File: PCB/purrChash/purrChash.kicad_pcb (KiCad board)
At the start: 2 copper layers, 39.5 x 70 mm, 6 parts

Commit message: some layout work - will probably change
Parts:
- added BT1: Battery_Cell, Connector_Wire:SolderWire-0.25sqmm_1x02_P4.2mm_D0.65mm_OD1.7mm, B.Cu at (15.1, 56.0)
- added C1: 10u, Capacitor_SMD:C_0805_2012Metric, B.Cu at (23.5, 59.5)
- added C2: 10u, Capacitor_SMD:C_0805_2012Metric, B.Cu at (26.5, 49.5)
- added C3: 100n, Capacitor_SMD:C_0603_1608Metric, B.Cu at (25.0, 59.5)
- added C4: 1u, Capacitor_SMD:C_0805_2012Metric, B.Cu at (10.5, 59.5)
- added C5: 1u, Capacitor_SMD:C_0805_2012Metric, B.Cu at (15.5, 59.5)
- added C7: 1u, Capacitor_SMD:C_0805_2012Metric, B.Cu at (21.5, 59.5)
- added D1: D_Schottky, Diode_SMD:D_0603_1608Metric, B.Cu at (24.5, 49.5)
- added D2: LED, LED_SMD:LED_2010_5025Metric_Pad1.52x2.65mm_HandSolder, B.Cu at (17.5, 17.5)
- added D3: LED, LED_SMD:LED_0805_2012Metric, B.Cu at (8.50, 17.5)
- added J1: USB4135-GF-A_REVA, Connector_USB:USB_C_Receptacle_GCT_USB4135-GF-A_6P_TopMnt_Horizontal, B.Cu at (13.0, 65.5)
- added M1: Motor_DC_ALT, Connector_Wire:SolderWire-0.25sqmm_1x02_P4.2mm_D0.65mm_OD1.7mm, F.Cu at (25.4, 46.0)
- added Q1: Q_NMOS_GSD, Package_TO_SOT_SMD:SOT-23, B.Cu at (29.5, 50.5)
- added R1: 100k, Resistor_SMD:R_0603_1608Metric, B.Cu at (28.5, 54.0)
- added R2: 1k, Resistor_SMD:R_0603_1608Metric, B.Cu at (20.5, 26.5)
- added R3: 1k, Resistor_SMD:R_0603_1608Metric, B.Cu at (19.0, 26.5)
- added R4: 1k, Resistor_SMD:R_0603_1608Metric, B.Cu at (30.5, 54.0)
- added R5: 5.1k, Resistor_SMD:R_0603_1608Metric, B.Cu at (8.00, 61.0)
- added R6: 5.1k, Resistor_SMD:R_0603_1608Metric, B.Cu at (20.0, 63.5)
- added U1: MSP430FR2110/MSP430FR2111, Package_SO:TSSOP-16_4.4x5mm_P0.65mm, B.Cu at (29.5, 60.0)
- added U2: MCP73811T-420I-OT, Package_TO_SOT_SMD:SOT-23-5, B.Cu at (12.9, 59.5)
- added U3: TPS7A0533PDBZR, Package_TO_SOT_SMD:SOT-23-5, B.Cu at (18.5, 59.5)
- ? (x3): moved to F.Cu
- ? (x2): moved to B.Cu
- moved ? 83.1 mm to (78.5, 27.2), turned to 180 degrees (x3)

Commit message: more pcb work
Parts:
- removed C7: 1u, Capacitor_SMD:C_0805_2012Metric
- added C6: 100n, Capacitor_SMD:C_0603_1608Metric, B.Cu at (43.1, 75.0)
- added D4: LED2, Library:LED_1206_3216Metric_shinethrough, B.Cu at (32.6, 31.2)
- added D5: LED3, Library:LED_1206_3216Metric_shinethrough, B.Cu at (24.7, 37.1)
- added D6: LED4, Library:LED_1206_3216Metric_shinethrough, B.Cu at (30.2, 37.1)
- added R10: 1k, Resistor_SMD:R_0603_1608Metric, B.Cu at (27.6, 32.2)
- added R11: 1k, Resistor_SMD:R_0603_1608Metric, B.Cu at (24.2, 39.3)
- added R12: 1k, Resistor_SMD:R_0603_1608Metric, B.Cu at (30.7, 39.3)
- added R7: 100k, Resistor_SMD:R_0603_1608Metric, B.Cu at (44.5, 64.0)
- added R8: 1k, Resistor_SMD:R_0603_1608Metric, B.Cu at (44.5, 65.5)
- added R9: 1k, Resistor_SMD:R_0603_1608Metric, B.Cu at (27.6, 33.7)
- added TP1: TouchPad, Connector_Wire:SolderWirePad_1x01_SMD_1x2mm, F.Cu at (26.4, 61.5)
- added TP2: TouchPad, Connector_Wire:SolderWirePad_1x01_SMD_1x2mm, F.Cu at (29.1, 55.2)
- added TP3: TouchPad, Connector_Wire:SolderWirePad_1x01_SMD_1x2mm, F.Cu at (22.8, 50.3)
- added TP4: TouchPad, Connector_Wire:SolderWirePad_1x01_SMD_1x2mm, F.Cu at (28.1, 45.9)
- C1, C2: value 10u -> 1u
- C3: value 100n -> 1u; footprint Capacitor_SMD:C_0603_1608Metric -> Capacitor_SMD:C_0805_2012Metric
- C4, C5: value 1u -> 10u
- D1: value D_Schottky -> CHG_LED; footprint Diode_SMD:D_0603_1608Metric -> LED_SMD:LED_0603_1608Metric
- D2: value LED -> D_Schottky; footprint LED_SMD:LED_2010_5025Metric_Pad1.52x2.65mm_HandSolder -> Diode_SMD:D_0603_1608Metric
- D3: value LED -> LED1; footprint LED_SMD:LED_0805_2012Metric -> Library:LED_1206_3216Metric_shinethrough
- M1: moved to B.Cu
- R1: value 100k -> 5.1k
- R2, R3, R4: value 1k -> 5.1k
- R6: value 5.1k -> 1k
- U1: value MSP430FR2110/MSP430FR2111 -> BQ21040DBV; footprint Package_SO:TSSOP-16_4.4x5mm_P0.65mm -> Package_TO_SOT_SMD:SOT-23-6
- U2: value MCP73811T-420I-OT -> TPS7A0533PDBZR
- U3: value TPS7A0533PDBZR -> MSP430FR2110/MSP430FR2111; footprint Package_TO_SOT_SMD:SOT-23-5 -> Package_SO:TSSOP-16_4.4x5mm_P0.65mm
- moved R2 52.8 mm to (35.1, 77.2), turned to 90 degrees
- moved D2 48.6 mm to (39.7, 60.7), turned to -90 degrees
- moved R3 48.1 mm to (30.8, 73.1)
- moved C4 36.9 mm to (43.1, 76.8), turned to 180 degrees
- moved U2 28.5 mm to (37.7, 73.6)
- moved U3 27.3 mm to (43.6, 70.2), turned to 90 degrees
- moved C5 26.3 mm to (41.7, 60.9)
- moved C2 25.3 mm to (34.8, 73.4)
- moved R1 24.6 mm to (20.4, 77.2)
- moved C3 21.4 mm to (37.7, 76.7), turned to 0 degrees
- moved D1 21.2 mm to (31.5, 69.5), turned to 0 degrees
- moved J1 20.2 mm to (27.8, 79.4)
- moved ? 20.2 mm to (14.8, 13.8) (x2)
- moved ? 20.2 mm to (14.7, 13.9)
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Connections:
- C1 pad 1: /3V3 -> /5V_USB
- C2 pad 1: /3V3 -> /VBAT
- C4 pad 1: /5V_USB -> /3V3
- C5 pad 1: /VBAT -> /3V3
- D1 pad 1: /3V3 -> CHG
- D1 pad 2: GND -> /CHG_LED
- D2 pad 1: /LED1_R -> /3V3
- D2 pad 2: /3V3 -> GND
- D3 pad 1: /LED2_R -> /LED1_R
- R1 pad 1: /MOTOR_MCU_R -> /CC2
- R2 pad 1: /LED1_R -> /CC1
- R2 pad 2: /LED_MCU -> GND
- R3 pad 1: /LED2_R -> /ISET
- R3 pad 2: /LED_MCU -> GND
- R4 pad 1: /MOTOR_MCU_R -> /TS
- R4 pad 2: /MOTOR_MCU -> /TS_R
- R5 pad 1: /CC2 -> /TS_R
- R6 pad 1: /CC1 -> /VBAT
- R6 pad 2: GND -> /CHG_LED
- U1 pad 1: unconnected-(U1-P1.1/UCA0CLK/ACLK/C1/A1-Pad1) -> /TS
- U1 pad 2: unconnected-(U1-P1.0/UCA0STE/SMCLK/C0/A1/Veref+-Pad2) -> /VBAT
- U1 pad 3: unconnected-(U1-TEST/SBWTCK-Pad3) -> CHG
- U1 pad 4: unconnected-(U1-NRST/NMI/SBWTDIO-Pad4) -> /ISET
- U1 pad 5: /3V3 -> GND
- U1 pad 6: GND -> /5V_USB
- U2 pad 1: /5V_USB -> /VBAT
- U2 pad 4: /5V_USB -> unconnected-(U2-NC-Pad4)
- U2 pad 5: GND -> /3V3
- U3 pad 1: /VBAT -> unconnected-(U3-P1.1/UCA0CLK/ACLK/C1/A1-Pad1)
- U3 pad 2: GND -> unconnected-(U3-P1.0/UCA0STE/SMCLK/C0/A1/Veref+-Pad2)
- U3 pad 3: /VBAT -> unconnected-(U3-TEST/SBWTCK-Pad3)
- U3 pad 4: unconnected-(U3-NC-Pad4) -> CHG
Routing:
- net /3V3: track 0.00 -> 118.5 mm
- net /LED_MCU1: track 0.00 -> 43.1 mm
- net /LED_MCU2: track 0.00 -> 37.7 mm
- net Net-(U3-P1.5/UCA0CLK/TMS/A5): track 0.00 -> 34.0 mm, vias 0 -> 1
- net Net-(U3-P1.6/UCA0RXD/UCA0SOMI/TB0.1/TDI/TCLK/A6): track 0.00 -> 32.0 mm, vias 0 -> 1
- net Net-(U3-P1.4/UCA0STE/TCK/A4): track 0.00 -> 24.9 mm, vias 0 -> 1
- net Net-(U3-P1.3/UCA0STE/TCK/A4): track 0.00 -> 24.2 mm, vias 0 -> 1
- net /VBAT: track 0.00 -> 21.5 mm
- net CHG: track 0.00 -> 19.4 mm
- net GND: track 0.00 -> 14.8 mm
- net /5V_USB: track 0.00 -> 8.11 mm
- net /CC2: track 0.00 -> 7.98 mm
- net /CC1: track 0.00 -> 7.90 mm
- net /LED1_R: track 0.00 -> 3.64 mm
- net /MOTOR_MCU_R: track 0.00 -> 3.31 mm
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- added copper zone on B.Cu, net GND
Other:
- outline, holes or cut-outs redrawn
- board text added: "&"
- board text added: "GalH"
- board text added: "TalyR"

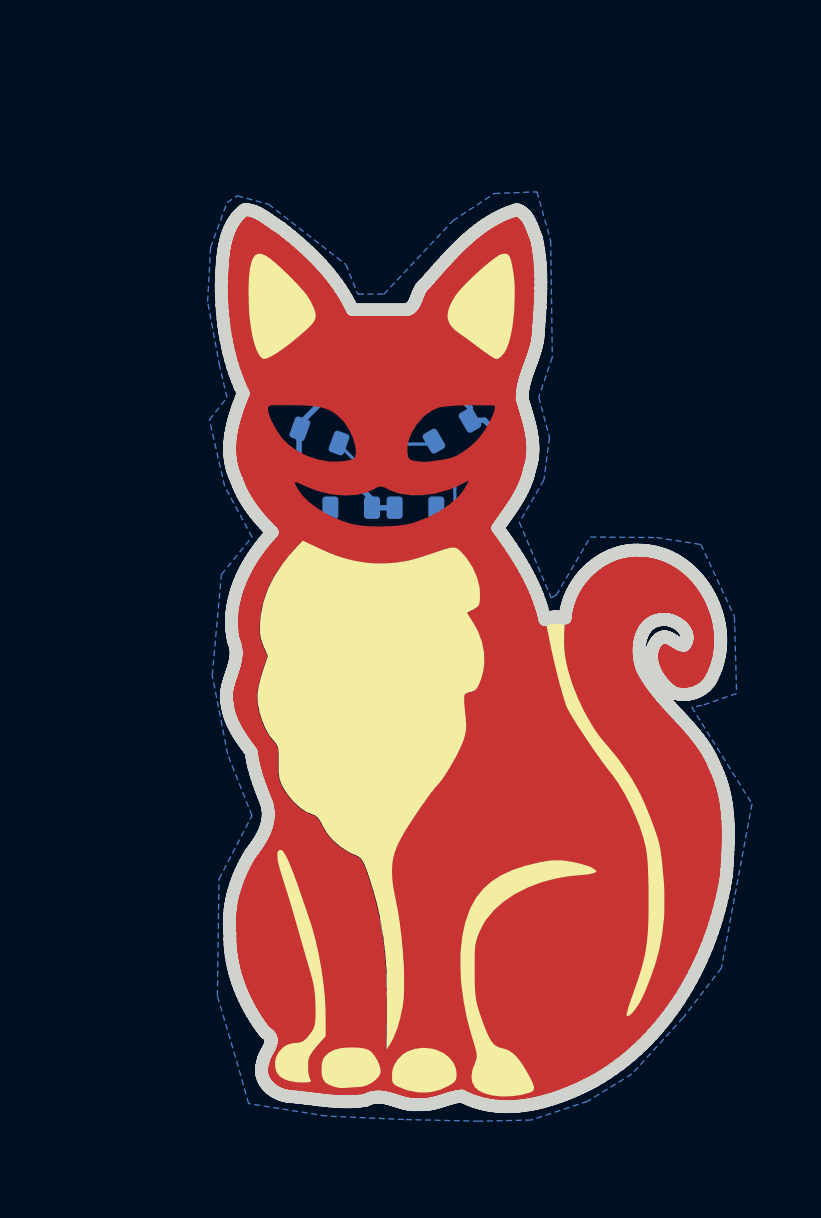
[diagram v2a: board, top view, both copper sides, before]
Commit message: pcb done with mouse-bite frame
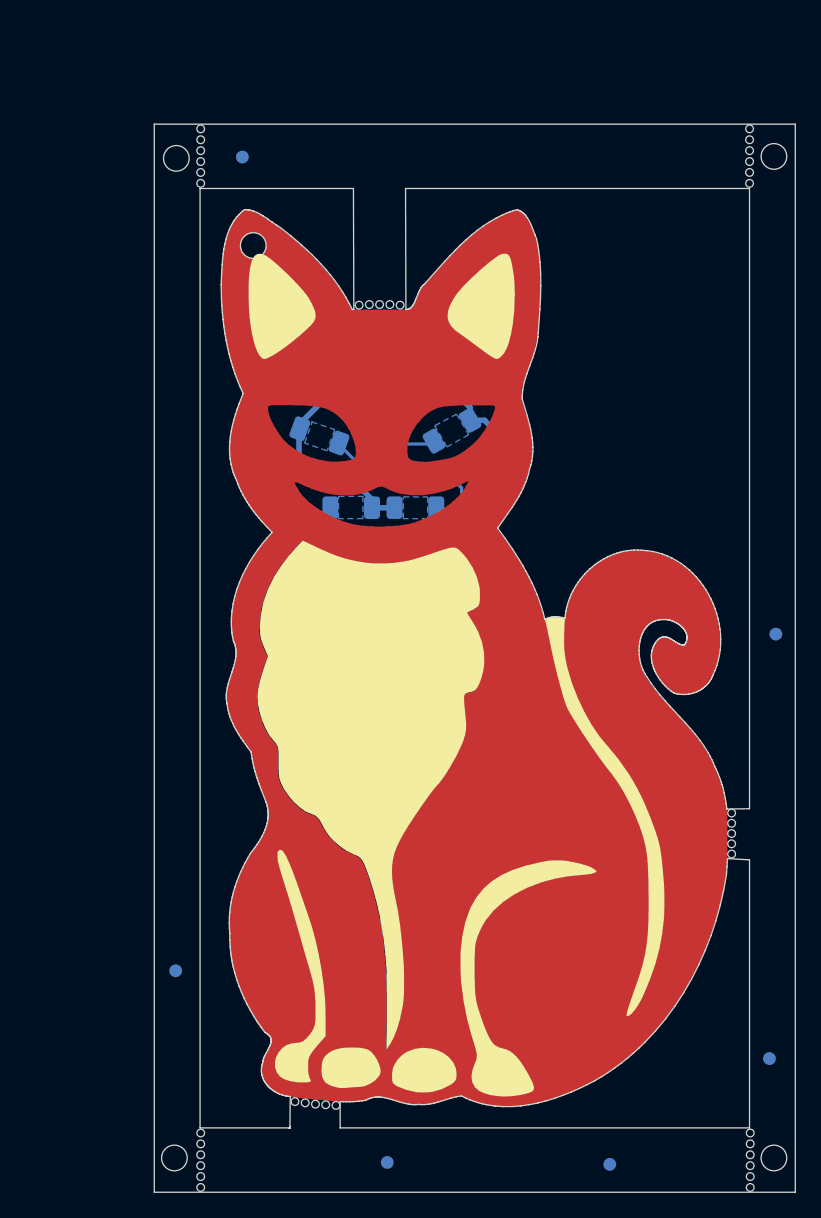
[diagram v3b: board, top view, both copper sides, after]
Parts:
- added ?: , , F.Cu at (56.0, 85.9)
- added ?: , , F.Cu at (13.2, 10.2)
- added ?: , , F.Cu at (13.2, 85.9)
- added ?: , , F.Cu at (56.0, 89.3)
- added ?: , , F.Cu at (56.0, 87.6)
- added ?: , , F.Cu at (13.2, 86.8)
- added ?: , , F.Cu at (13.2, 87.6)
- added ?: , , F.Cu at (56.0, 88.5)
- added ?: , , F.Cu at (13.2, 89.3)
- added ?: , , F.Cu at (13.2, 11.0)
- added ?: , , F.Cu at (13.2, 90.2)
- added ?: , , F.Cu at (13.2, 11.8)
- added ?: , , F.Cu at (13.2, 9.30)
- added ?: , , F.Cu at (56.0, 90.2)
- added ?: , , F.Cu at (56.0, 86.8)
- added ?: , , F.Cu at (13.2, 7.60)
- added ?: , , F.Cu at (13.2, 8.45)
- added ?: , , F.Cu at (13.2, 88.5)
- added J2: Conn_01x03_Pin, Connector_PinHeader_2.00mm:PinHeader_1x03_P2.00mm_Vertical, B.Cu at (48.1, 67.5)
- added REF**: tollin_hole_2mm, Library:tollin_hole_2mm, F.Cu at (11.2, 87.8)
- added REF**: mouse_bite, Library:mouse_bite, F.Cu at (26.4, 21.3)
- added REF**: tollin_hole_2mm, Library:tollin_hole_2mm, F.Cu at (57.9, 87.8)
- added REF**: mouse_bite, Library:mouse_bite, F.Cu at (22.1, 83.7)
- added REF**: mouse_bite, Library:mouse_bite, F.Cu at (54.6, 63.4)
- added REF**: mouse_bite, Library:mouse_bite, F.Cu at (20.6, 83.5)
- added REF**: mouse_bite, Library:mouse_bite, F.Cu at (54.6, 64.2)
- added REF**: mouse_bite, Library:mouse_bite, F.Cu at (21.4, 83.5)
- added REF**: tollin_hole_2mm, Library:tollin_hole_2mm, F.Cu at (11.3, 9.90)
- added REF**: mouse_bite, Library:mouse_bite, F.Cu at (56.0, 11.8)
- added REF**: mouse_bite, Library:mouse_bite, F.Cu at (27.1, 21.3)
- added REF**: mouse_bite, Library:mouse_bite, F.Cu at (28.8, 21.4)
- added REF**: mouse_bite, Library:mouse_bite, F.Cu at (54.6, 62.5)
- added REF**: mouse_bite, Library:mouse_bite, F.Cu at (27.9, 21.3)
- added REF**: mouse_bite, Library:mouse_bite, F.Cu at (54.6, 61.8)
- added REF**: mouse_bite, Library:mouse_bite, F.Cu at (56.0, 10.2)
- added REF**: tollin_hole_2mm, Library:tollin_hole_2mm, F.Cu at (57.9, 9.75)
- added REF**: mouse_bite, Library:mouse_bite, F.Cu at (56.0, 11.0)
- added REF**: mouse_bite, Library:mouse_bite, F.Cu at (56.0, 8.45)
- added REF**: Fiducial_1mm_Mask2mm, Fiducial:Fiducial_1mm_Mask2mm, B.Cu at (11.2, 73.2)
- added REF**: Fiducial_1mm_Mask2mm, Fiducial:Fiducial_1mm_Mask2mm, B.Cu at (57.5, 80.1)
- added REF**: Fiducial_1mm_Mask2mm, Fiducial:Fiducial_1mm_Mask2mm, B.Cu at (16.4, 9.80)
- added REF**: mouse_bite, Library:mouse_bite, F.Cu at (54.6, 61.0)
- added REF**: Fiducial_1mm_Mask2mm, Fiducial:Fiducial_1mm_Mask2mm, B.Cu at (27.8, 88.2)
- added REF**: Fiducial_1mm_Mask2mm, Fiducial:Fiducial_1mm_Mask2mm, B.Cu at (45.1, 88.3)
- added REF**: Fiducial_1mm_Mask2mm, Fiducial:Fiducial_1mm_Mask2mm, B.Cu at (58.0, 47.0)
- added REF**: mouse_bite, Library:mouse_bite, F.Cu at (56.0, 9.30)
- added REF**: tollin_hole_2mm, Library:tollin_hole_2mm, F.Cu at (17.3, 16.7)
- added REF**: mouse_bite, Library:mouse_bite, F.Cu at (22.9, 83.7)
- added REF**: mouse_bite, Library:mouse_bite, F.Cu at (23.8, 83.8)
- added REF**: mouse_bite, Library:mouse_bite, F.Cu at (25.6, 21.4)
- added REF**: mouse_bite, Library:mouse_bite, F.Cu at (56.0, 7.60)
- moved TP3 3.33 mm to (26.1, 49.7)
- moved TP4 1.63 mm to (27.4, 44.5)
- moved J1 0.25 mm to (27.8, 79.6)
- moved R1 0.25 mm to (20.4, 77.5)
- moved R2 0.25 mm to (35.1, 77.4)
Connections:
- U3 pad 3: unconnected-(U3-TEST/SBWTCK-Pad3) -> /SBWTCK
- U3 pad 4: CHG -> /SBWTDIO
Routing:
- net CHG: track 19.4 -> 1.60 mm
- net /SBWTDIO: track 0.00 -> 6.00 mm
- net /SBWTCK: track 0.00 -> 4.52 mm
- net Net-(U3-P1.6/UCA0RXD/UCA0SOMI/TB0.1/TDI/TCLK/A6): track 32.0 -> 34.7 mm
- net Net-(U3-P1.5/UCA0CLK/TMS/A5): track 34.0 -> 32.9 mm
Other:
- board size 39.5 x 70 mm -> 50 x 83.3 mm

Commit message: update BOM and fix some DNP and footprints
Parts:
- C6: footprint Capacitor_SMD:C_0603_1608Metric -> Capacitor_SMD:C_0402_1005Metric
- Q1: value Q_NMOS_GSD -> NXV55UNR
- U2: value TPS7A0533PDBZR -> TPS70933DBVR
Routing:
- net /3V3: track 118.1 -> 119.7 mm

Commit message: many changes😅
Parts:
- moved D2 7.71 mm to (47.4, 60.0), turned to 180 degrees
- moved M1 7.28 mm to (47.6, 57.6), turned to 180 degrees
- moved C5 5.55 mm to (47.2, 61.9), turned to 180 degrees
- moved Q1 1.03 mm to (43.6, 61.0)
- moved R7 1.03 mm to (43.5, 63.9)
- moved R8 1.03 mm to (43.5, 65.4)
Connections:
- C5 pad 2: GND -> /MOTOR_GND
- D2 pad 2: GND -> /MOTOR_GND
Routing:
- net /3V3: track 119.7 -> 111.6 mm
- net GND: track 14.7 -> 8.71 mm
- net /MOTOR_GND: track 2.71 -> 7.68 mm
